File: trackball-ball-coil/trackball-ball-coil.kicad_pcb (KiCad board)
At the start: 2 copper layers, 22 x 22 mm, 4 parts, among them J1 WIRE-3

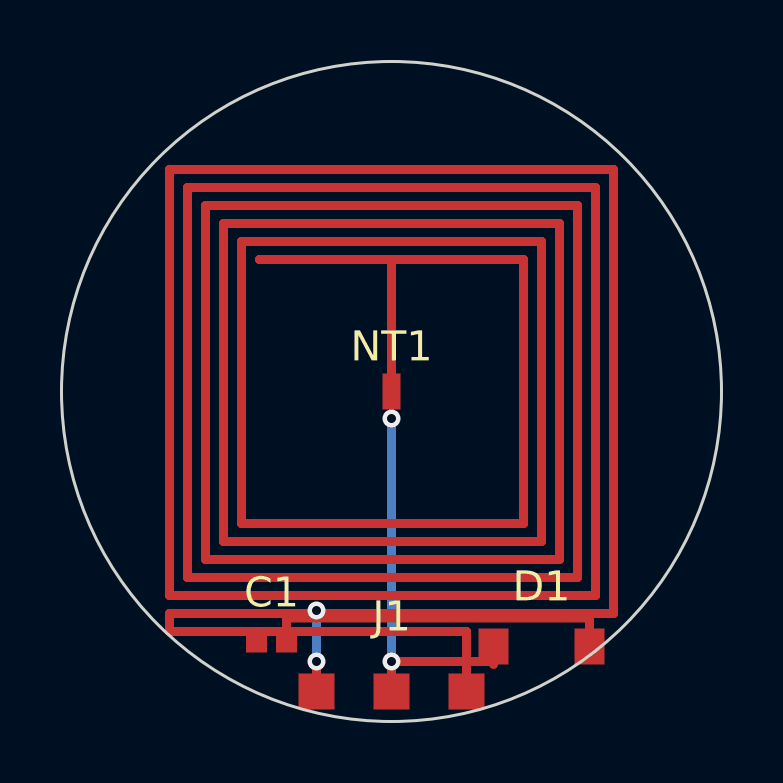
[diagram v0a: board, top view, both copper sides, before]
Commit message: ball: driver-preserved WIP (2026-10-11 recovery, ANT cascade owner-pending)
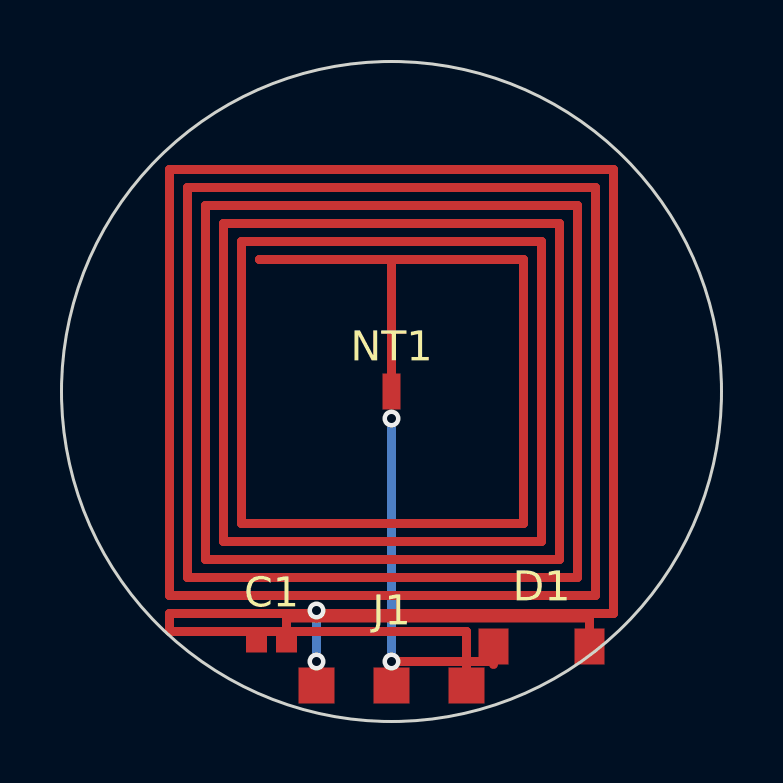
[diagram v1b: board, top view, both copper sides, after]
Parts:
- moved J1 0.20 mm to (100.0, 109.8)
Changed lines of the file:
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@@
   (segment (start 92.6 107.4) (end 92.6 108) (width 0.3) (layer "F.Cu") (net 3 "RX_A"))
   (segment (start 92.6 108) (end 102.5 108) (width 0.3) (layer "F.Cu") (net 3 "RX_A"))
-  (segment (start 102.5 108) (end 102.5 109.4) (width 0.3) (layer "F.Cu") (net 3 "RX_A"))
+  (segment (start 102.5 108) (end 102.5 109.2) (width 0.3) (layer "F.Cu") (net 3 "RX_A"))
   (segment (start 96.5 107.55) (end 106.6 107.55) (width 0.3) (layer "F.Cu") (net 2 "VIN_RX"))
   (segment (start 96.5 107.55) (end 96.5 107.9) (width 0.3) (layer "F.Cu") (net 2 "VIN_RX"))
@@
   (footprint "trackball-ball-coil:WIREPADS-3" (version 20250114) (generator "pcbnew") (generator_version "10.0")
     (layer "F.Cu")
-    (at 100 110)
-    (descr "J1 wire-solder SMD pads to main J2 (top edge, tight to outline v0.1)")
+    (at 100 109.8)
+    (descr "J1 wire-solder SMD pads to main J2 (top edge; moved 110->109.8: J1.3-copper 0.04 over r11 edge)")
     (tags "wire")
     (property "Reference" "J1" (at 0 -2.5 0) (layer "F.SilkS") (effects (font (size 1 1) (thickness 0.15))))
